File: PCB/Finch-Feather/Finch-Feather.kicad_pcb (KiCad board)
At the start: 2 copper layers, 61 x 22.9 mm, 0 parts

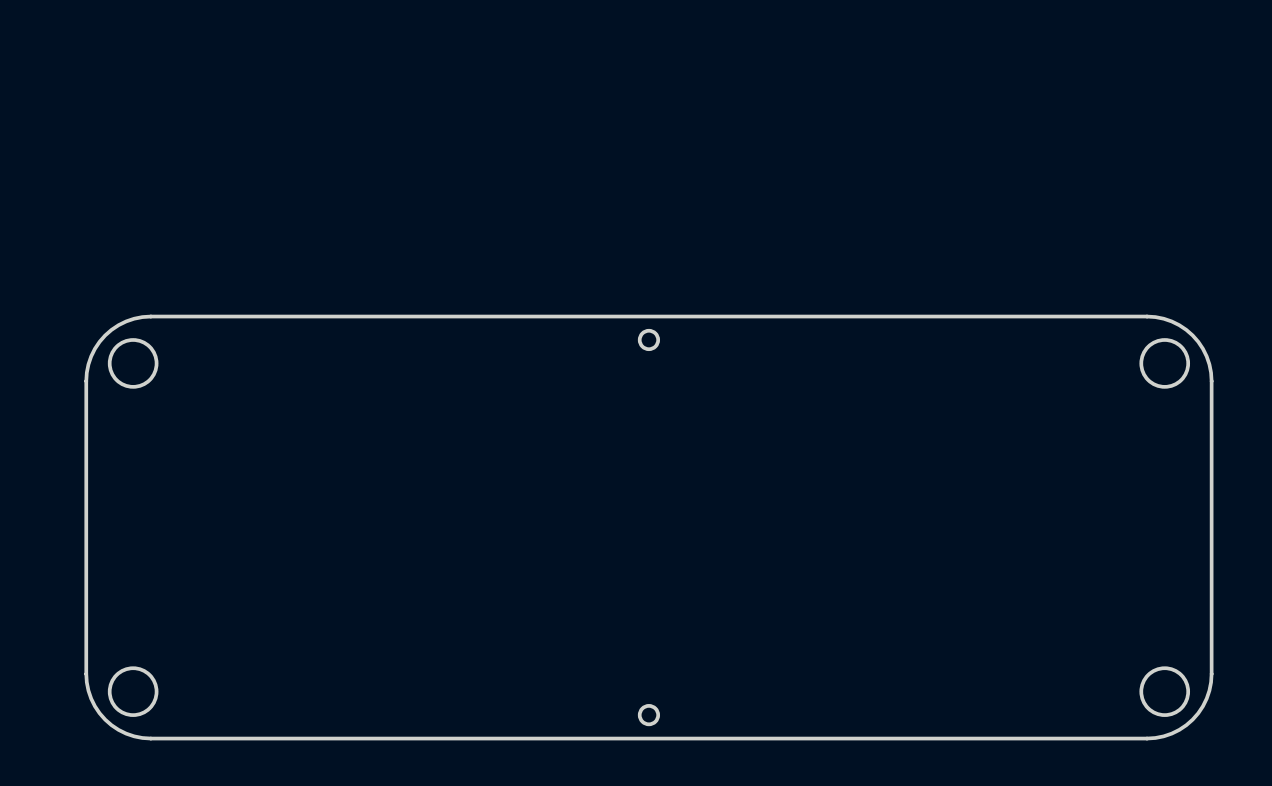
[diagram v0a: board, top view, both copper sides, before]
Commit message: PCB
PCB started, next step figuring out which pins on module to use
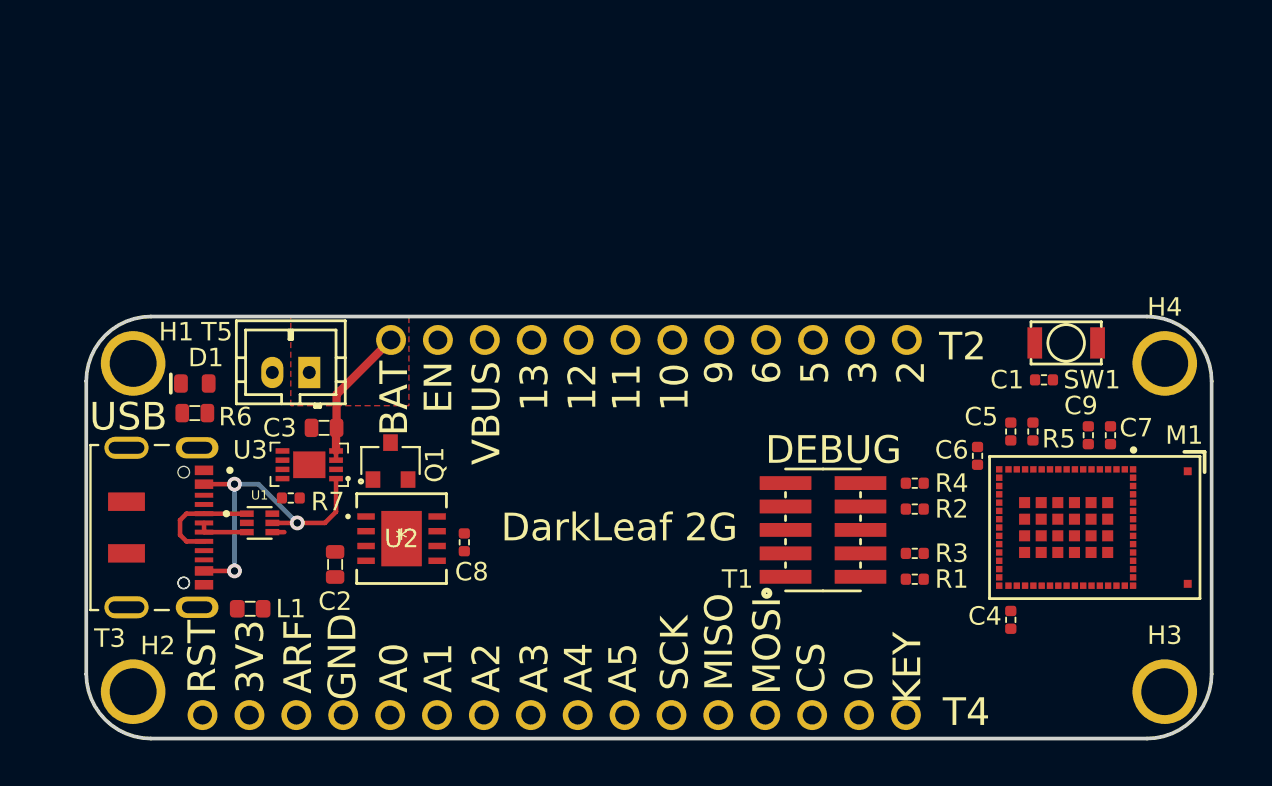
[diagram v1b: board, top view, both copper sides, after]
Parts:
- added C1: C0402C104K9PACTU, AVR-KiCAD-Lib-Resistors:R0402, F.Cu at (171.4, 92.0)
- added C2: C0603C475K9PACTU, AVR-KiCAD-Lib-Capacitors:C0603, F.Cu at (133.0, 102.0)
- added C3: C0603C475K9PACTU, AVR-KiCAD-Lib-Capacitors:C0603, F.Cu at (132.4, 94.6)
- added C4: C0402C104K9PACTU, AVR-KiCAD-Lib-Resistors:R0402, F.Cu at (169.6, 105.0)
- added C5: C0402C104K9PACTU, AVR-KiCAD-Lib-Resistors:R0402, F.Cu at (169.6, 94.8)
- added C6: C0402C104K9PACTU, AVR-KiCAD-Lib-Resistors:R0402, F.Cu at (167.8, 96.1)
- added C7: C0402C104K9PACTU, AVR-KiCAD-Lib-Resistors:R0402, F.Cu at (175.0, 95.0)
- added C8: C0402C104K9PACTU, AVR-KiCAD-Lib-Resistors:R0402, F.Cu at (140.0, 100.8)
- added C9: C0402C104K9PACTU, AVR-KiCAD-Lib-Resistors:R0402, F.Cu at (173.8, 95.0)
- added D1: LTST-C194TBKT, AVR-KiCAD-Lib-Diodes:LED0603, F.Cu at (125.4, 92.2)
- added H1: 2.54mm_PLT_Hole, AVR-KiCAD-Lib-Holes_Fasteners:2.54mm_PLT_Hole, F.Cu at (122.1, 91.1)
- added H2: 2.54mm_PLT_Hole, AVR-KiCAD-Lib-Holes_Fasteners:2.54mm_PLT_Hole, F.Cu at (122.1, 108.9)
- added H3: 2.54mm_PLT_Hole, AVR-KiCAD-Lib-Holes_Fasteners:2.54mm_PLT_Hole, F.Cu at (177.9, 108.9)
- added H4: 2.54mm_PLT_Hole, AVR-KiCAD-Lib-Holes_Fasteners:2.54mm_PLT_Hole, F.Cu at (177.9, 91.1)
- added L1: MI0603K300R-10, AVR-KiCAD-Lib-Inductors:MI0603K300R-10, F.Cu at (128.4, 104.4)
- added M1: STM32WB5MMGH6TR, AVR-KiCAD-Lib-Modules:STM32WB5MMGH6TR, F.Cu at (172.6, 100.0)
- added Q1: DMP3125L-7, growbox-KiCAD-Transistors:SOT-23, F.Cu at (136.0, 96.4)
- added R1: RC0402FR-0710KL, AVR-KiCAD-Lib-Resistors:R0402, F.Cu at (164.4, 102.8)
- added R2: RC0402FR-0710KL, AVR-KiCAD-Lib-Resistors:R0402, F.Cu at (164.4, 99.0)
- added R3: RC0402FR-0710KL, AVR-KiCAD-Lib-Resistors:R0402, F.Cu at (164.4, 101.4)
- added R4: RC0402FR-0710KL, AVR-KiCAD-Lib-Resistors:R0402, F.Cu at (164.4, 97.6)
- added R5: RC0402FR-0710KL, AVR-KiCAD-Lib-Resistors:R0402, F.Cu at (170.8, 94.8)
- added R6: RC0603FR-07470RL, AVR-KiCAD-Lib-Resistors:R0603, F.Cu at (125.4, 93.8)
- added R7: RC0402FR-072KL, AVR-KiCAD-Lib-Resistors:R0402, F.Cu at (130.6, 98.4)
- added SW1: B3U-1000P, AVR-KiCAD-Lib-Mech-Switches:B3U-1000P, F.Cu at (172.6, 90.0)
- added T1: 20021121-00010C4LF, AVR-KiCAD-Lib-Connectors:20021121-00010C4LF, F.Cu at (159.4, 100.1)
- added T2: TSW-112-07-G-S, AVR-KiCAD-Lib-Connectors:SAMTEC-TSW-112-07-X-S, F.Cu at (150.0, 89.8)
- added T3: DX07S016JA1R1500, AVR-KiCAD-Lib-Connectors:JAE_DX07S016JA1R1500, F.Cu at (124.8, 100.0)
- added T4: TSW-116-07-L-S, AVR-KiCAD-Lib-Connectors:SAMTEC-TSW-116-07-X-S, F.Cu at (144.9, 110.2)
- added T5: B2B-PH-K-S(LF)(SN), AVR-KiCAD-Lib-Connectors:B2B-PH-K-S(LF)(SN), F.Cu at (131.6, 91.6)
- added U1: USBLC6-2P6, AVR-KiCAD-Lib-ICs:SOT50P160X60-6N, F.Cu at (128.9, 99.8)
- added U2: TLV1117-33IDRJR, AVR-KiCAD-Lib-ICs:TLV1117-33IDRJR, F.Cu at (136.6, 100.6)
- added U3: MCP73831T-2ACI_MC, AVR-KiCAD-Lib-ICs:MCP73831T-2ACI-MC, F.Cu at (131.6, 96.6)
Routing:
- net +5V: track 0.00 -> 17.8 mm, vias 0 -> 3
- net /VBAT: track 0.00 -> 7.74 mm
- net Net-(T3-Pad5): track 0.00 -> 6.01 mm
- net Net-(T3-Pad6): track 0.00 -> 2.82 mm
- net /USB_D+: track 0.00 -> 0.65 mm
- added copper zone on In2.Cu, net +3V3
- added copper zone on F.Cu, net /VBAT
- added copper zone on In1.Cu, net GND
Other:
- outline, holes or cut-outs redrawn
- copper layers 2 -> 4
- board text added: "0"
- board text added: "10"
- board text added: "11"
- board text added: "12"
- board text added: "13"
- board text added: "2"
- board text added: "3"
- board text added: "3V3"
- board text added: "5"
- board text added: "6"
- board text added: "9"
- board text added: "A0"
- board text added: "A1"
- board text added: "A2"
- board text added: "A3"
- board text added: "A4"
- board text added: "A5"
- board text added: "ARF"
- board text added: "BAT"
- board text added: "CS"
- board text added: "DEBUG"
- board text added: "DarkLeaf 2G"
- board text added: "EN"
- board text added: "GND"
- board text added: "KEY"
- board text added: "MISO"
- board text added: "MOSI"
- board text added: "RST"
- board text added: "SCK"
- board text added: "USB"
- board text added: "VBUS"

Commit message: PCB Near Finished
Head signals wired to pins on module, power supply section and USB connector are next
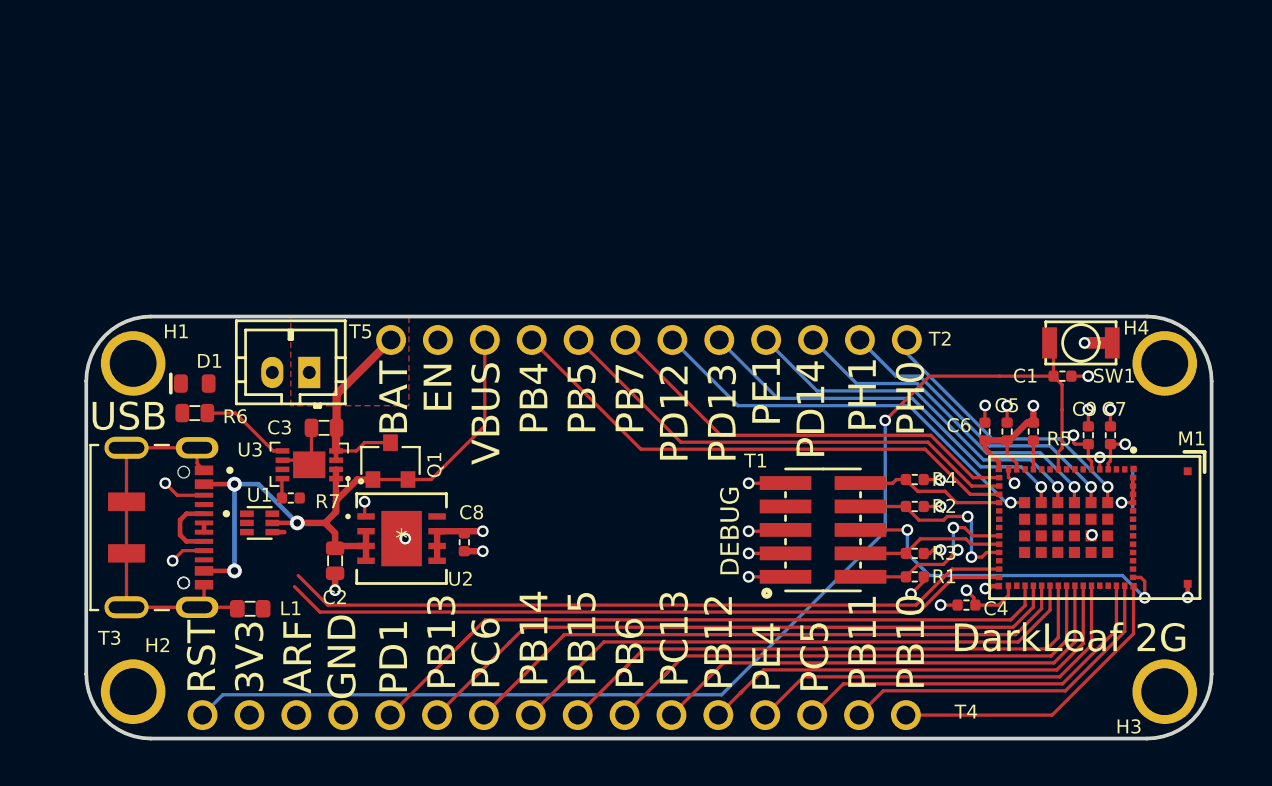
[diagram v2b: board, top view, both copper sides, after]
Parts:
- moved C4 2.53 mm to (167.2, 104.2), turned to 180 degrees
- moved C6 1.38 mm to (168.2, 94.8)
- moved C1 1.02 mm to (172.4, 91.8)
- moved SW1 0.80 mm to (173.4, 90.0)
- moved C2 0.20 mm to (133.0, 101.8)
- moved C5 0.20 mm to (169.4, 94.8)
- moved R4 0.20 mm to (164.4, 97.4)
- moved R2 0.14 mm to (164.4, 98.9)
- moved R1 0.13 mm to (164.4, 102.7)
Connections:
- M1 pad 18: Net-(M1-Pad18) -> /PB7
- M1 pad 19: Net-(M1-Pad19) -> /PB5
- M1 pad 20: Net-(M1-Pad20) -> /PB4
- M1 pad 34: Net-(M1-Pad34) -> /PD1
- M1 pad 35: Net-(M1-Pad35) -> /PB13
- M1 pad 36: Net-(M1-Pad36) -> /PC6
- M1 pad 37: Net-(M1-Pad37) -> /PB14
- M1 pad 38: Net-(M1-Pad38) -> /PB15
- M1 pad 39: Net-(M1-Pad39) -> /PB6
- M1 pad 40: Net-(M1-Pad40) -> /PC13
- M1 pad 41: Net-(M1-Pad41) -> /PB12
- M1 pad 42: Net-(M1-Pad42) -> /PE4
- M1 pad 45: Net-(M1-Pad45) -> /PC5
- M1 pad 46: Net-(M1-Pad46) -> /PB11
- M1 pad 47: Net-(M1-Pad47) -> /PB10
- M1 pad 61: Net-(M1-Pad61) -> /PH0
- M1 pad 62: Net-(M1-Pad62) -> /PH1
- M1 pad 63: Net-(M1-Pad63) -> /PD14
- M1 pad 64: Net-(M1-Pad64) -> /PE1
- M1 pad 65: Net-(M1-Pad65) -> /PD13
- M1 pad 66: Net-(M1-Pad66) -> /PD12
- T2 pad 10: Net-(T2-Pad10) -> /PD14
- T2 pad 11: Net-(T2-Pad11) -> /PH1
- T2 pad 12: Net-(T2-Pad12) -> /PH0
- T2 pad 4: Net-(T2-Pad4) -> /PB4
- T2 pad 5: Net-(T2-Pad5) -> /PB5
- T2 pad 6: Net-(T2-Pad6) -> /PB7
- T2 pad 7: Net-(T2-Pad7) -> /PD12
- T2 pad 8: Net-(T2-Pad8) -> /PD13
- T2 pad 9: Net-(T2-Pad9) -> /PE1
- T4 pad 10: Net-(T4-Pad10) -> /PB6
- T4 pad 11: Net-(T4-Pad11) -> /PC13
- T4 pad 12: Net-(T4-Pad12) -> /PB12
- T4 pad 13: Net-(T4-Pad13) -> /PE4
- T4 pad 14: Net-(T4-Pad14) -> /PC5
- T4 pad 15: Net-(T4-Pad15) -> /PB11
- T4 pad 16: Net-(T4-Pad16) -> /PB10
- T4 pad 5: Net-(T4-Pad5) -> /PD1
- T4 pad 6: Net-(T4-Pad6) -> /PB13
- T4 pad 7: Net-(T4-Pad7) -> /PC6
- T4 pad 8: Net-(T4-Pad8) -> /PB14
- T4 pad 9: Net-(T4-Pad9) -> /PB15
- U1 pad 1: Net-(T3-Pad5) -> Net-(T3-Pad6)
- U1 pad 3: Net-(T3-Pad6) -> Net-(T3-Pad5)
- U1 pad 4: /USB_D+ -> /USB_D-
- U1 pad 6: /USB_D- -> /USB_D+
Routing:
- net /NRST: track 0.00 -> 66.4 mm, vias 0 -> 1
- net /USB_D-: track 0.00 -> 40.2 mm
- net /PD1: track 0.00 -> 38.9 mm
- net /USB_D+: track 0.65 -> 39.4 mm
- net /PB13: track 0.00 -> 35.9 mm
- net /PC6: track 0.00 -> 33.9 mm
- net /PB14: track 0.00 -> 32.1 mm
- net /PB15: track 0.00 -> 31.5 mm
- net GND: track 0.00 -> 29.7 mm, vias 0 -> 23
- net /PB6: track 0.00 -> 29.0 mm
- net /PB4: track 0.00 -> 28.8 mm
- net /PC13: track 0.00 -> 26.5 mm
- net /PB5: track 0.00 -> 26.1 mm
- net +3V3: track 0.00 -> 25.4 mm, vias 0 -> 9
- net /PB12: track 0.00 -> 24.7 mm
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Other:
- net class Default: trace_width 0.25 -> 0.1778; via_dia 0.8 -> 0.635; via_drill 0.4 -> 0.381
- rule pad_to_mask_clearance: 0 -> 0.0508
- rule trace_min: 0.2 -> 0.1778
- board text added: "PB10"
- board text added: "PB11"
- board text added: "PB12"
- board text added: "PB13"
- board text added: "PB14"
- board text added: "PB15"
- board text added: "PB4"
- board text added: "PB5"
- board text added: "PB6"
- board text added: "PB7"
- board text added: "PC13"
- board text added: "PC5"
- board text added: "PC6"
- board text added: "PD1"
- board text added: "PD12"
- board text added: "PD13"
- board text added: "PD14"
- board text added: "PE1"
- board text added: "PE4"
- board text added: "PH0"
- board text added: "PH1"
- board text removed: "0"
- board text removed: "10"
- board text removed: "11"
- board text removed: "12"
- board text removed: "13"
- board text removed: "2"
- board text removed: "3"
- board text removed: "5"
- board text removed: "6"
- board text removed: "9"
- board text removed: "A0"
- board text removed: "A1"
- board text removed: "A2"
- board text removed: "A3"
- board text removed: "A4"
- board text removed: "A5"
- board text removed: "CS"
- board text removed: "KEY"
- board text removed: "MISO"
- board text removed: "MOSI"
- board text removed: "SCK"

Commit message: PCB Progress
More progress on PCB design, made some tweaks and changes, implemented enable circuit.
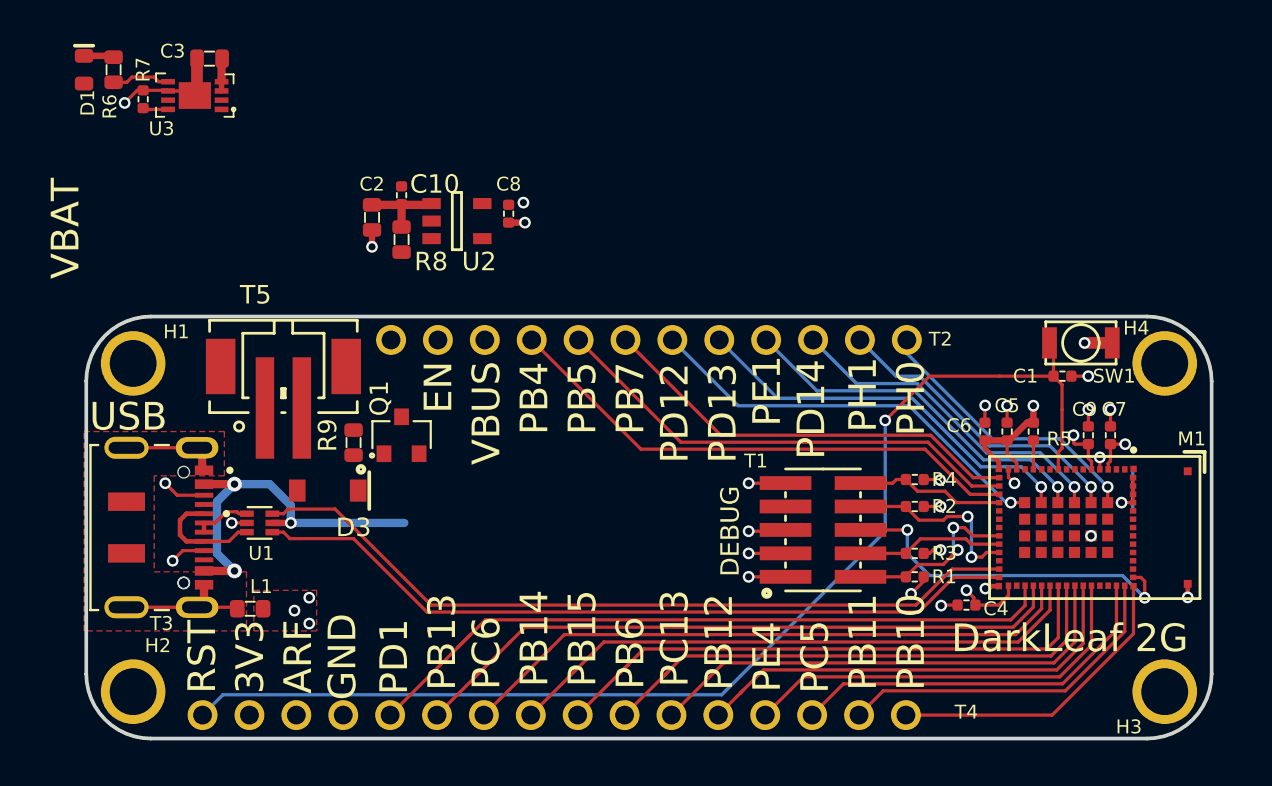
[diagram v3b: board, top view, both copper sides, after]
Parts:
- added C10: C0402C104K9PACTU, AVR-KiCAD-Lib-Resistors:R0402, F.Cu at (136.6, 82.0)
- added D3: MBR0540T1G, AVR-KiCAD-Lib-Diodes:D_SOD-123, F.Cu at (132.6, 98.0)
- added R8: RC0603FR-07100KL, AVR-KiCAD-Lib-Resistors:R0603, F.Cu at (136.6, 84.4)
- added R9: RC0603FR-07100KL, AVR-KiCAD-Lib-Resistors:R0603, F.Cu at (134.0, 95.4)
- T5: value B2B-PH-K-S(LF)(SN) -> S2B-PH-SM4-TB(LF)(SN); footprint AVR-KiCAD-Lib-Connectors:B2B-PH-K-S(LF)(SN) -> AVR-KiCAD-Lib-Connectors:B2B-PH-SM4-TB(LF)(SN)
- U2: value TLV1117-33IDRJR -> TLV75533PDBVR; footprint AVR-KiCAD-Lib-ICs:TLV1117-33IDRJR -> AVR-KiCAD-Lib-ICs:TLV75533PDBVR
- moved R7 23.0 mm to (122.6, 76.8), turned to 90 degrees
- moved C3 20.9 mm to (126.2, 74.6)
- moved U3 20.9 mm to (125.4, 76.6)
- moved R6 19.1 mm to (121.0, 75.2), turned to 270 degrees
- moved C2 18.7 mm to (135.0, 83.2)
- moved D1 18.0 mm to (119.4, 75.2), turned to 90 degrees
- moved C8 18.0 mm to (142.4, 83.0)
- moved U2 17.5 mm to (139.6, 83.4)
- moved T5 1.61 mm to (130.2, 92.4), turned to 0 degrees
- moved Q1 1.52 mm to (136.6, 95.0)
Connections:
- C2 pad 2: +5V -> VCC
- D1 pad 1: +5V -> VCC
- Q1 pad 1: +5V -> VBUS
- Q1 pad 2: +5V -> VCC
- T2 pad 2: Net-(T2-Pad2) -> /ENABLE
- T2 pad 3: +5V -> VBUS
- T3 pad 11: +5V -> VBUS
- T3 pad 2: +5V -> VBUS
- T5 pad 1: /VBAT -> GND
- T5 pad 2: GND -> /VBAT
- U1 pad 5: +5V -> VBUS
- U2 pad 1: GND -> VCC
- U2 pad 2: +5V -> GND
- U2 pad 3: +5V -> /ENABLE
- U2 pad 4: +5V -> Net-(U2-Pad4)
- U3 pad 1: +5V -> VCC
- U3 pad 2: +5V -> VCC
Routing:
- net +5V: track 38.4 -> 0.00 mm, vias 3 -> 0
- net VBUS: track 0.00 -> 20.4 mm, vias 0 -> 3
- net /VBAT: track 10.9 -> 1.72 mm
- net Net-(L1-Pad2): track 21.2 -> 12.7 mm
- net VCC: track 0.00 -> 4.49 mm
- net +3V3: track 25.4 -> 21.3 mm
- net /USB_D+: track 39.4 -> 42.4 mm
- net Net-(T3-Pad6): track 0.50 -> 3.12 mm
- net GND: track 29.7 -> 32.3 mm, vias 23 -> 26
- net Net-(T3-Pad5): track 3.69 -> 6.22 mm
- net /USB_D-: track 40.2 -> 41.9 mm
- net /STAT: track 4.92 -> 3.37 mm
- net /LED: track 0.00 -> 1.53 mm
- added copper zone on F.Cu, net GND
- added copper zone on F.Cu, net Net-(L1-Pad2)
- removed copper zone on F.Cu, net /VBAT
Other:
- board text added: "SPARKFUN WILL STEAL THIS!"
- board text added: "VBAT"
- board text removed: "BAT"
